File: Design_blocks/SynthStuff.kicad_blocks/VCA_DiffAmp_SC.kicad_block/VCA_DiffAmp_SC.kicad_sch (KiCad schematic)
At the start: 18 parts, among them Q1 BC548, Q2 BC548, U1 TL072

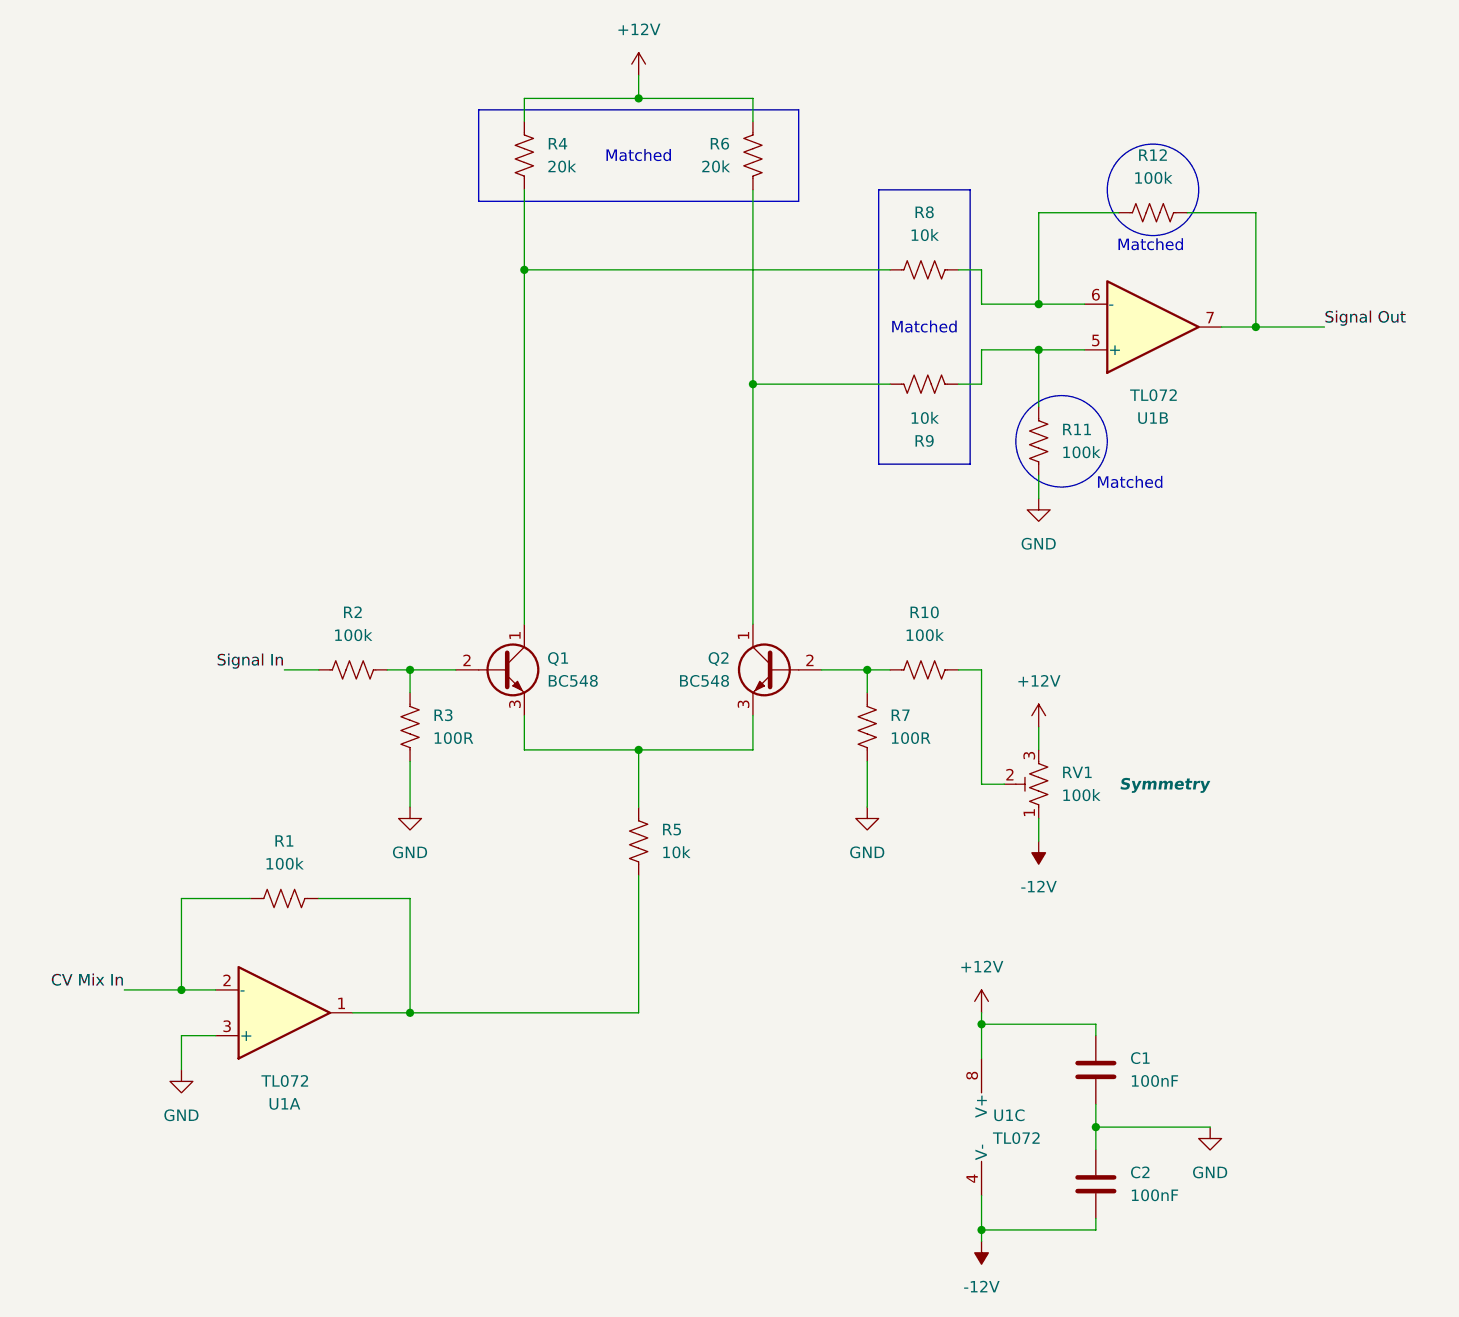
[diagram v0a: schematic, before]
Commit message: VCA minor updates after Mk2 submodule PCB design
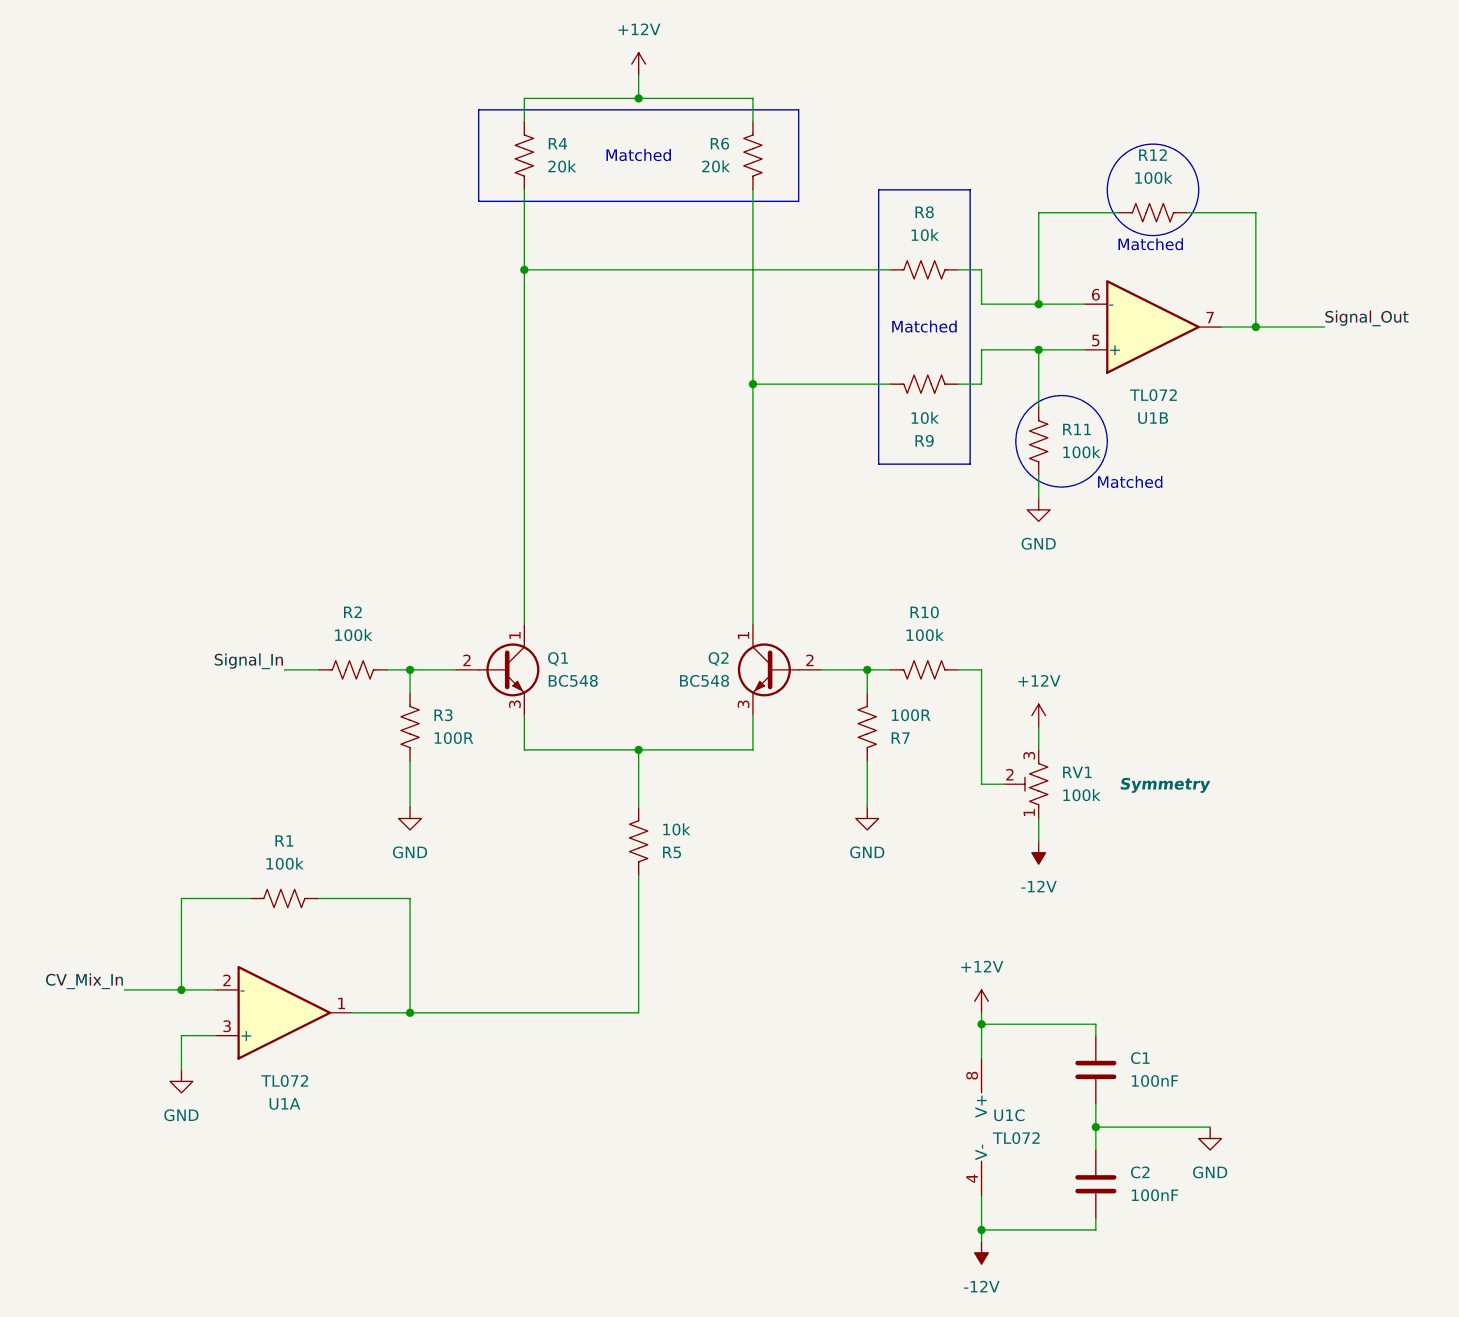
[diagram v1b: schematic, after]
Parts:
- R1, R10, R11, R12, R2, R3, R4, R5, R6, R7, R8, R9: footprint Resistor_THT:R_Axial_DIN0207_L6.3mm_D2.5mm_P7.62mm_Horizontal -> Resistor_THT:R_Axial_DIN0207_L6.3mm_D2.5mm_P2.54mm_Vertical
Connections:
- net GND: now also R7.2; no longer R7.1
- net at R1.2, U1.1: now also R5.2; no longer R5.1
- net at Q1.3 (E), Q2.3 (E): now also R5.1; no longer R5.2
- net at R10.1: now also Q2.2 (B), R7.1; no longer RV1.2
- net CV Mix In renamed CV_Mix_In
- net Signal In renamed Signal_In
- net Signal Out renamed Signal_Out
- new net: R10.2, RV1.2
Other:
- moved on the sheet: R10, R5, R7
